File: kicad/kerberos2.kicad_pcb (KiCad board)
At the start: 2 copper layers, 62.5 x 83.8 mm, 15 parts, among them J1 USB4125-GF-A_REVA2, J2 MIDI-in, J3 MIDI-thru, J4 MIDI-out, SW1 TL1105JAF160Q, U1 RP2040, U2 W9812G6KH-6, U3 T8Q144, U4 MX25L25645G

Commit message: first complete test version for Kerberos 2
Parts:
- removed @HOLE0: , 
- removed U$1: , midi:CE-4MM
- removed U$2: , midi:MUELLTONNE_10.00
- removed the U1 at (100.4, 92.0)
- added C1: 100n, Capacitor_SMD:C_0805_2012Metric, F.Cu at (63.7, 79.7)
- added C10: 100n, Capacitor_SMD:C_0805_2012Metric, F.Cu at (63.1, 29.4)
- added C11: 100n, Capacitor_SMD:C_0805_2012Metric, F.Cu at (63.1, 26.4)
- added C12: 100n, Capacitor_SMD:C_0805_2012Metric, F.Cu at (67.6, 23.4)
- added C13: 100n, Capacitor_SMD:C_0805_2012Metric, F.Cu at (138.6, 26.5)
- added C14: 1u, Capacitor_SMD:C_0805_2012Metric, F.Cu at (63.1, 32.5)
- added C15: 4.7u, Capacitor_SMD:C_0805_2012Metric, F.Cu at (27.6, 52.9)
- added C16: 100n, Capacitor_SMD:C_0402_1005Metric, F.Cu at (36.0, 105.9)
- added C17: 100n, Capacitor_SMD:C_0402_1005Metric, F.Cu at (27.6, 58.9)
- added C18: 100n, Capacitor_SMD:C_0402_1005Metric, F.Cu at (33.0, 107.9)
- added C19: 100n, Capacitor_SMD:C_0402_1005Metric, F.Cu at (32.0, 58.9)
- added C2: 10u, Capacitor_SMD:C_0805_2012Metric, F.Cu at (63.1, 23.4)
- added C20: 100n, Capacitor_SMD:C_0402_1005Metric, F.Cu at (27.6, 55.9)
- added C21: 100n, Capacitor_SMD:C_0402_1005Metric, F.Cu at (18.6, 55.6)
- added C22: 100n, Capacitor_SMD:C_0402_1005Metric, F.Cu at (30.1, 107.9)
- added C23: 100n, Capacitor_SMD:C_0402_1005Metric, F.Cu at (23.1, 58.9)
- added C24: 100n, Capacitor_SMD:C_0402_1005Metric, F.Cu at (10.9, 86.4)
- added C25: 100n, Capacitor_SMD:C_0402_1005Metric, F.Cu at (18.6, 61.7)
- added C26: 100n, Capacitor_SMD:C_0402_1005Metric, F.Cu at (23.2, 52.9)
- added C27: 100n, Capacitor_SMD:C_0402_1005Metric, F.Cu at (18.6, 58.6)
- added C28: 100n, Capacitor_SMD:C_0402_1005Metric, F.Cu at (23.1, 55.9)
- added C29: 100n, Capacitor_SMD:C_0402_1005Metric, F.Cu at (32.0, 55.9)
- added C3: 100n, Capacitor_SMD:C_0805_2012Metric, F.Cu at (125.1, 33.9)
- added C30: 100n, Capacitor_SMD:C_0402_1005Metric, F.Cu at (32.1, 52.9)
- added C31: 100n, Capacitor_SMD:C_0402_1005Metric, F.Cu at (132.3, 93.4)
- added C32: 100n, Capacitor_SMD:C_0402_1005Metric, F.Cu at (128.1, 81.4)
- added C33: 100n, Capacitor_SMD:C_0402_1005Metric, F.Cu at (136.8, 90.4)
- added C34: 4.7u, Capacitor_SMD:C_0805_2012Metric, F.Cu at (50.4, 75.3)
- added C35: 10u, Capacitor_SMD:C_0805_2012Metric, F.Cu at (59.1, 81.2)
- added C36: 4.7u, Capacitor_SMD:C_0805_2012Metric, F.Cu at (59.6, 93.0)
- added C37: 10u, Capacitor_SMD:C_0805_2012Metric, F.Cu at (51.4, 87.2)
- added C38: 1n, Capacitor_SMD:C_0805_2012Metric, F.Cu at (148.0, 44.0)
- added C39: 1n, Capacitor_SMD:C_0805_2012Metric, F.Cu at (135.0, 58.7)
- added C4: 100n, Capacitor_SMD:C_0805_2012Metric, F.Cu at (67.6, 26.4)
- added C40: 100n, Capacitor_SMD:C_0805_2012Metric, F.Cu at (153.6, 40.7)
- added C41: 100n, Capacitor_SMD:C_0805_2012Metric, F.Cu at (147.2, 47.3)
- added C5: 100n, Capacitor_SMD:C_0805_2012Metric, F.Cu at (125.1, 30.8)
- added C6: 100n, Capacitor_SMD:C_0805_2012Metric, F.Cu at (129.6, 33.7)
- added C7: 100n, Capacitor_SMD:C_0805_2012Metric, F.Cu at (72.0, 23.4)
- added C8: 100n, Capacitor_SMD:C_0805_2012Metric, F.Cu at (134.0, 33.7)
- added C9: 1u, Capacitor_SMD:C_0805_2012Metric, F.Cu at (138.6, 29.6)
- added D3: ~, LED_THT:LED_D3.0mm, F.Cu at (69.2, 57.8)
- added D4: ~, LED_THT:LED_D3.0mm, F.Cu at (87.5, 57.8)
- added D5: BAV99, Package_TO_SOT_SMD:SOT-23, F.Cu at (130.3, 59.4)
- added D6: BAV99, Package_TO_SOT_SMD:SOT-23, F.Cu at (142.6, 48.0)
- added D7: BAV99, Package_TO_SOT_SMD:SOT-23, F.Cu at (139.7, 52.9)
- added FB1: FerriteBead, Inductor_SMD:L_0805_2012Metric, F.Cu at (77.8, 77.2)
- added FB2: FerriteBead, Inductor_SMD:L_0805_2012Metric, F.Cu at (18.7, 52.8)
- added JP2: host-mode-supply, Connector_PinHeader_2.54mm:PinHeader_1x02_P2.54mm_Vertical, F.Cu at (86.5, 22.6)
- added JP3: 3.3V+, Connector_PinHeader_2.54mm:PinHeader_1x02_P2.54mm_Vertical, F.Cu at (22.2, 90.5)
- added JP4: 3.3V, Connector_PinHeader_2.54mm:PinHeader_1x02_P2.54mm_Vertical, F.Cu at (26.8, 90.5)
- added JP5: 3.3V-, Connector_PinHeader_2.54mm:PinHeader_1x02_P2.54mm_Vertical, F.Cu at (26.8, 83.3)
- added JP6: 1.2V+, Connector_PinHeader_2.54mm:PinHeader_1x02_P2.54mm_Vertical, F.Cu at (31.5, 83.3)
- added JP7: 1.2V, Connector_PinHeader_2.54mm:PinHeader_1x02_P2.54mm_Vertical, F.Cu at (36.1, 83.3)
- added JP8: 1.2V-, Connector_PinHeader_2.54mm:PinHeader_1x02_P2.54mm_Vertical, F.Cu at (22.2, 83.3)
- added JP9: ~{USB_BOOT}, Connector_PinHeader_2.54mm:PinHeader_1x02_P2.54mm_Vertical, F.Cu at (134.0, 27.4)
- added L1: 4.7u, coil:coil, F.Cu at (59.5, 76.1)
- added L2: 4.7u, coil:coil, F.Cu at (51.2, 92.0)
- added Q1: Q_NMOS_GSD, Package_TO_SOT_SMD:SOT-23, F.Cu at (150.7, 108.0)
- added Q10: Q_NMOS_GSD, Package_TO_SOT_SMD:SOT-23, F.Cu at (147.7, 93.0)
- added Q2: Q_NMOS_GSD, Package_TO_SOT_SMD:SOT-23, F.Cu at (144.1, 73.2)
- added Q3: Q_NMOS_GSD, Package_TO_SOT_SMD:SOT-23, F.Cu at (132.7, 69.6)
- added Q4: Q_NMOS_GSD, Package_TO_SOT_SMD:SOT-23, F.Cu at (118.2, 111.1)
- added Q5: Q_NMOS_GSD, Package_TO_SOT_SMD:SOT-23, F.Cu at (38.9, 32.0)
- added Q6: Q_NMOS_GSD, Package_TO_SOT_SMD:SOT-23, F.Cu at (25.3, 31.4)
- added Q7: Q_NMOS_GSD, Package_TO_SOT_SMD:SOT-23, F.Cu at (135.3, 111.1)
- added Q8: Q_NMOS_GSD, Package_TO_SOT_SMD:SOT-23, F.Cu at (154.6, 78.4)
- added Q9: Q_NMOS_GSD, Package_TO_SOT_SMD:SOT-23, F.Cu at (156.3, 66.3)
- added R1: 5.1, Resistor_SMD:R_0805_2012Metric, F.Cu at (91.1, 21.8)
- added R10: 22, Resistor_SMD:R_0805_2012Metric, F.Cu at (95.5, 21.8)
- added R11: 22, Resistor_SMD:R_0805_2012Metric, F.Cu at (99.6, 27.6)
- added R12: 22, Resistor_SMD:R_0805_2012Metric, F.Cu at (104.3, 24.7)
- added R13: 22, Resistor_SMD:R_0805_2012Metric, F.Cu at (95.2, 33.5)
- added R14: 22, Resistor_SMD:R_0805_2012Metric, F.Cu at (99.9, 21.8)
- added R15: 22, Resistor_SMD:R_0805_2012Metric, F.Cu at (104.0, 27.6)
- added R16: 22, Resistor_SMD:R_0805_2012Metric, F.Cu at (108.7, 24.7)
- added R17: 22, Resistor_SMD:R_0805_2012Metric, F.Cu at (99.6, 30.6)
- added R18: 22, Resistor_SMD:R_0805_2012Metric, F.Cu at (95.2, 27.6)
- added R19: 22, Resistor_SMD:R_0805_2012Metric, F.Cu at (108.7, 21.8)
- added R2: 5.1, Resistor_SMD:R_0805_2012Metric, F.Cu at (91.1, 24.7)
- added R20: 1k, Resistor_SMD:R_0805_2012Metric, F.Cu at (104.3, 21.8)
- added R21: 1k, Resistor_SMD:R_0805_2012Metric, F.Cu at (90.8, 31.9)
- added R22: 10k, Resistor_SMD:R_0805_2012Metric, F.Cu at (143.0, 26.6)
- added R23: 10k, Resistor_SMD:R_0805_2012Metric, F.Cu at (138.4, 33.7)
- added R24: 1k, Resistor_SMD:R_0805_2012Metric, F.Cu at (67.5, 29.4)
- added R25: 10k, Resistor_SMD:R_0805_2012Metric, F.Cu at (72.0, 26.4)
- added R26: 10k, Resistor_SMD:R_0402_1005Metric, F.Cu at (30.1, 105.9)
- added R27: 10k, Resistor_SMD:R_0402_1005Metric, F.Cu at (118.1, 66.1)
- added R28: 10k, Resistor_SMD:R_0402_1005Metric, F.Cu at (33.1, 105.9)
- added R29: 10k, Resistor_SMD:R_0402_1005Metric, F.Cu at (118.1, 70.1)
- added R3: 27, Resistor_SMD:R_0805_2012Metric, F.Cu at (81.6, 81.9)
- added R30: 10k, Resistor_SMD:R_0402_1005Metric, F.Cu at (118.1, 68.1)
- added R31: 10k, Resistor_SMD:R_0402_1005Metric, F.Cu at (121.0, 68.1)
- added R32: 10k, Resistor_SMD:R_0402_1005Metric, F.Cu at (121.0, 66.1)
- added R33: 10k, Resistor_SMD:R_0402_1005Metric, F.Cu at (132.3, 102.3)
- added R34: 10k, Resistor_SMD:R_0402_1005Metric, F.Cu at (136.8, 93.4)
- added R35: 1k, Resistor_SMD:R_0402_1005Metric, F.Cu at (132.3, 99.3)
- added R36: 1k, Resistor_SMD:R_0402_1005Metric, F.Cu at (132.3, 96.4)
- added R37: 10k, Resistor_SMD:R_0402_1005Metric, F.Cu at (136.7, 99.3)
- added R38: 10k, Resistor_SMD:R_0402_1005Metric, F.Cu at (136.8, 96.3)
- added R39: 10k, Resistor_SMD:R_0402_1005Metric, F.Cu at (149.7, 111.2)
- added R4: 27, Resistor_SMD:R_0805_2012Metric, F.Cu at (95.2, 30.6)
- added R40: R, Resistor_SMD:R_0402_1005Metric, F.Cu at (55.0, 79.0)
- added R41: R, Resistor_SMD:R_0402_1005Metric, F.Cu at (51.0, 79.0)
- added R42: R, Resistor_SMD:R_0402_1005Metric, F.Cu at (55.5, 89.6)
- added R43: R, Resistor_SMD:R_0402_1005Metric, F.Cu at (59.9, 89.6)
- added R44: 220, Resistor_SMD:R_1206_3216Metric, F.Cu at (134.5, 52.3)
- added R45: 220, Resistor_SMD:R_1206_3216Metric, F.Cu at (134.5, 55.6)
- added R46: 220, Resistor_SMD:R_1206_3216Metric, F.Cu at (125.0, 58.6)
- added R47: 220, Resistor_SMD:R_1206_3216Metric, F.Cu at (148.5, 40.8)
- added R48: 220, Resistor_SMD:R_1206_3216Metric, F.Cu at (142.9, 44.1)
- added R49: 10k, Resistor_SMD:R_0805_2012Metric, F.Cu at (139.5, 56.5)
- added R5: 27, Resistor_SMD:R_0805_2012Metric, F.Cu at (99.9, 24.7)
- added R50: 220, Resistor_SMD:R_1206_3216Metric, F.Cu at (119.4, 58.6)
- added R51: 220, Resistor_SMD:R_1206_3216Metric, F.Cu at (142.9, 40.8)
- added R52: 1k8, Resistor_SMD:R_0805_2012Metric, F.Cu at (152.4, 43.9)
- added R53: 3k3, Resistor_SMD:R_0805_2012Metric, F.Cu at (144.4, 51.7)
- added R54: 10k, Resistor_SMD:R_0402_1005Metric, F.Cu at (143.1, 76.5)
- added R55: 10k, Resistor_SMD:R_0402_1005Metric, F.Cu at (131.7, 72.8)
- added R56: 10k, Resistor_SMD:R_0402_1005Metric, F.Cu at (117.2, 114.3)
- added R57: 10k, Resistor_SMD:R_0402_1005Metric, F.Cu at (37.9, 35.2)
- added R58: 10k, Resistor_SMD:R_0402_1005Metric, F.Cu at (24.3, 34.6)
- added R59: 10k, Resistor_SMD:R_0402_1005Metric, F.Cu at (134.3, 114.3)
- added R6: 27, Resistor_SMD:R_0805_2012Metric, F.Cu at (86.4, 28.9)
- added R60: 10k, Resistor_SMD:R_0402_1005Metric, F.Cu at (153.6, 81.6)
- added R61: 10k, Resistor_SMD:R_0402_1005Metric, F.Cu at (155.4, 69.5)
- added R62: 10k, Resistor_SMD:R_0402_1005Metric, F.Cu at (146.7, 96.2)
- added R7: 22, Resistor_SMD:R_0805_2012Metric, F.Cu at (86.4, 31.9)
- added R8: 22, Resistor_SMD:R_0805_2012Metric, F.Cu at (90.8, 28.9)
- added R9: 22, Resistor_SMD:R_0805_2012Metric, F.Cu at (95.5, 24.7)
- added RN1: 33, resistor-network:16P8, F.Cu at (63.0, 108.3)
- added RN2: 33, resistor-network:16P8, F.Cu at (68.9, 108.3)
- added RN3: 33, resistor-network:16P8, F.Cu at (84.5, 108.8)
- added RN4: 33, resistor-network:16P8, F.Cu at (75.3, 108.3)
- added RN5: 33, resistor-network:16P8, F.Cu at (91.8, 109.0)
- added SW2: SKRPADE010, button:KEY-SMD_4P-L4.2-W3.2-P2.20-LS4.6, F.Cu at (119.8, 31.5)
- added U10: 6N138, 6N138S:6N138S, F.Cu at (60.0, 65.9)
- added U11: 74LS14, Package_SO:SOIC-14_3.9x8.7mm_P1.27mm, F.Cu at (70.4, 76.4)
- added U4: 74ALVC164245DGG,51, Package_SO:TSSOP-48_8x12.5mm_P0.5mm, F.Cu at (88.9, 96.2)
- added U5: GW1NR-4&4B_QN881, qn88:QFN-88_EP_10x10_Pitch0.4mm, F.Cu at (71.5, 86.9)
- added U6: AD8694ARZ, Package_SO:SOIC-14_3.9x8.7mm_P1.27mm, F.Cu at (99.2, 64.2)
- added U7: TMCS1108A3UQDR, Package_SO:SOIC-8_3.9x4.9mm_P1.27mm, F.Cu at (88.9, 68.4)
- added U8: M3406, Package_TO_SOT_SMD:TSOT-23-5, F.Cu at (54.3, 75.3)
- added U9: M3406, Package_TO_SOT_SMD:TSOT-23-5, F.Cu at (55.8, 93.0)
- added USB1: TYPEC-304J-BCP16, usb-c:USB-C-SMD_TYPEC-304J-BCP16, F.Cu at (102.6, 89.1)
- added X1: SX3M12.000M20F30TNN, oscillator:SX3M12.000M20F30TNN, F.Cu at (81.3, 78.0)
- D1, D2: value LED -> D_Schottky; footprint LED_THT:LED_D3.0mm -> Diode_SMD:D_SMA
- J1: value USB4125-GF-A_REVA2 -> 503398-1892; footprint usb-c:GCT_USB4125-GF-A_REVA2 -> sd-card:MOLEX_503398-1892
- SW1: value TL1105JAF160Q -> side-button
- U2: value W9812G6KH-6 -> RP2040; footprint Package_SO:TSOP-II-54_22.2x10.16mm_P0.8mm -> rp2040:QFN40P700X700X90-57N
- U3: value T8Q144 -> 74ALVC164245DGG,51; footprint Package_QFP:LQFP-144_20x20mm_P0.5mm -> Package_SO:TSSOP-48_8x12.5mm_P0.5mm
- moved D2 56.9 mm to (54.3, 104.0), turned to -90 degrees
- moved D1 52.9 mm to (100.3, 100.6), turned to 90 degrees
- moved U2 32.3 mm to (88.9, 81.2)
- moved U1 12.5 mm to (78.6, 68.7)
- moved U3 10.9 mm to (70.7, 99.9), turned to 90 degrees
- moved J1 5.22 mm to (100.6, 76.0)
- moved J4 0.05 mm to (95.3, 50.2)
- renumbered U4 to U1
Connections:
- D1 pad 1: unconnected-(D1-Pad1) -> +5V
- D1 pad 2: unconnected-(D1-Pad2) -> Net-(D1-Pad2)
- D2 pad 1: unconnected-(D2-Pad1) -> +5V
- D2 pad 2: unconnected-(D2-Pad2) -> Net-(D2-Pad2)
- J2 pad 4: unconnected-(J2-Pad4) -> Net-(J2-Pad4)
- J2 pad 5: unconnected-(J2-Pad5) -> Net-(D5-Pad1)
- J3 pad 2: unconnected-(J3-Pad2) -> GND
- J3 pad 4: unconnected-(J3-Pad4) -> Net-(J3-Pad4)
- J3 pad 5: unconnected-(J3-Pad5) -> Net-(C38-Pad1)
- J3 pad S: unconnected-(J3-PadS) -> GND
- J4 pad 2: unconnected-(J4-Pad2) -> GND
- J4 pad 4: unconnected-(J4-Pad4) -> Net-(J4-Pad4)
- J4 pad 5: unconnected-(J4-Pad5) -> Net-(C39-Pad1)
- J4 pad S: unconnected-(J4-PadS) -> GND
- JP1 pad 1: unconnected-(JP1-Pad1) -> GND
- JP1 pad 10: unconnected-(JP1-Pad10) -> Net-(JP1-Pad10)
- JP1 pad 11: unconnected-(JP1-Pad11) -> Net-(JP1-Pad11)
- JP1 pad 12: unconnected-(JP1-Pad12) -> Net-(JP1-Pad12)
- JP1 pad 13: unconnected-(JP1-Pad13) -> Net-(JP1-Pad13)
- JP1 pad 14: unconnected-(JP1-Pad14) -> Net-(JP1-Pad14)
- JP1 pad 15: unconnected-(JP1-Pad15) -> Net-(JP1-Pad15)
- JP1 pad 16: unconnected-(JP1-Pad16) -> Net-(JP1-Pad16)
- JP1 pad 17: unconnected-(JP1-Pad17) -> Net-(JP1-Pad17)
- JP1 pad 18: unconnected-(JP1-Pad18) -> Net-(JP1-Pad18)
- JP1 pad 19: unconnected-(JP1-Pad19) -> Net-(JP1-Pad19)
- JP1 pad 2: unconnected-(JP1-Pad2) -> Net-(D2-Pad2)
- JP1 pad 20: unconnected-(JP1-Pad20) -> Net-(JP1-Pad20)
- JP1 pad 21: unconnected-(JP1-Pad21) -> Net-(JP1-Pad21)
- JP1 pad 22: unconnected-(JP1-Pad22) -> GND
- JP1 pad 3: unconnected-(JP1-Pad3) -> Net-(D2-Pad2)
- JP1 pad 4: unconnected-(JP1-Pad4) -> Net-(JP1-Pad4)
- JP1 pad 5: unconnected-(JP1-Pad5) -> Net-(JP1-Pad5)
- JP1 pad 6: unconnected-(JP1-Pad6) -> Net-(JP1-Pad6)
- JP1 pad 7: unconnected-(JP1-Pad7) -> Net-(JP1-Pad7)
- JP1 pad 8: unconnected-(JP1-Pad8) -> Net-(JP1-Pad8)
- JP1 pad 9: unconnected-(JP1-Pad9) -> Net-(JP1-Pad9)
- JP1 pad A: unconnected-(JP1-PadA) -> GND
- JP1 pad B: unconnected-(JP1-PadB) -> Net-(JP1-PadB)
- JP1 pad C: unconnected-(JP1-PadC) -> Net-(JP1-PadC)
- JP1 pad D: unconnected-(JP1-PadD) -> Net-(JP1-PadD)
- JP1 pad E: unconnected-(JP1-PadE) -> Net-(JP1-PadE)
- JP1 pad F: unconnected-(JP1-PadF) -> Net-(JP1-PadF)
- JP1 pad H: unconnected-(JP1-PadH) -> Net-(JP1-PadH)
- JP1 pad J: unconnected-(JP1-PadJ) -> Net-(JP1-PadJ)
- JP1 pad K: unconnected-(JP1-PadK) -> Net-(JP1-PadK)
- JP1 pad L: unconnected-(JP1-PadL) -> Net-(JP1-PadL)
- JP1 pad M: unconnected-(JP1-PadM) -> Net-(JP1-PadM)
- JP1 pad N: unconnected-(JP1-PadN) -> Net-(JP1-PadN)
- JP1 pad P: unconnected-(JP1-PadP) -> Net-(JP1-PadP)
- JP1 pad R: unconnected-(JP1-PadR) -> Net-(JP1-PadR)
- JP1 pad S: unconnected-(JP1-PadS) -> Net-(JP1-PadS)
- JP1 pad T: unconnected-(JP1-PadT) -> Net-(JP1-PadT)
- JP1 pad U: unconnected-(JP1-PadU) -> Net-(JP1-PadU)
- JP1 pad V: unconnected-(JP1-PadV) -> Net-(JP1-PadV)
- JP1 pad W: unconnected-(JP1-PadW) -> Net-(JP1-PadW)
- JP1 pad X: unconnected-(JP1-PadX) -> Net-(JP1-PadX)
- JP1 pad Y: unconnected-(JP1-PadY) -> Net-(JP1-PadY)
- JP1 pad Z: unconnected-(JP1-PadZ) -> GND
- SW1 pad 1: unconnected-(SW1-Pad1) -> GND
- SW1 pad 2: unconnected-(SW1-Pad2) -> Net-(R22-Pad2)
- U1 pad 1: unconnected-(U4-Pad1) -> /GW1NR FPGA/FLASH_CS
- U1 pad 2: unconnected-(U4-Pad2) -> /GW1NR FPGA/FLASH-SIO1
- U1 pad 3: unconnected-(U4-Pad3) -> /GW1NR FPGA/FLASH-SIO2
- U1 pad 4: unconnected-(U4-Pad4) -> GND
- U1 pad 5: unconnected-(U4-Pad5) -> /GW1NR FPGA/FLASH-SIO0
- U1 pad 6: unconnected-(U4-Pad6) -> /GW1NR FPGA/FLASH-SCLK
- U1 pad 7: unconnected-(U4-Pad7) -> /GW1NR FPGA/FLASH-SIO3
- U1 pad 8: unconnected-(U4-Pad8) -> +3.3V
- U2 pad 1: Net-(U2-Pad1) -> +3.3V
- U2 pad 10: unconnected-(U2-Pad10) -> +3.3V
- U2 pad 11: unconnected-(U2-Pad11) -> /RP2040 microcontroller/spare2
- U2 pad 12: Net-(U2-Pad12) -> /RP2040 microcontroller/spare3
- U2 pad 13: unconnected-(U2-Pad13) -> /RP2040 microcontroller/spare4
- U2 pad 14: Net-(U2-Pad1) -> /RP2040 microcontroller/spare5
- U2 pad 15: unconnected-(U2-Pad15) -> /RP2040 microcontroller/spare6
- U2 pad 16: unconnected-(U2-Pad16) -> Net-(R22-Pad2)
- U2 pad 19: unconnected-(U2-Pad19) -> GND
- U2 pad 2: unconnected-(U2-Pad2) -> /RP2040 microcontroller/JTAGSEL_N
- U2 pad 20: unconnected-(U2-Pad20) -> /RP2040 microcontroller/XIN
- U2 pad 22: unconnected-(U2-Pad22) -> +3.3V
- U2 pad 23: unconnected-(U2-Pad23) -> /RP2040 microcontroller/1.1V
- U2 pad 26: unconnected-(U2-Pad26) -> Net-(R23-Pad1)
- U2 pad 27: Net-(U2-Pad1) -> unconnected-(U2-Pad27)
- U2 pad 28: Net-(U2-Pad28) -> unconnected-(U2-Pad28)
- U2 pad 3: Net-(U2-Pad3) -> /RP2040 microcontroller/TCK
- U2 pad 30: unconnected-(U2-Pad30) -> Net-(J1-Pad3)
- U2 pad 31: unconnected-(U2-Pad31) -> Net-(J1-Pad5)
- U2 pad 32: unconnected-(U2-Pad32) -> Net-(J1-Pad7)
- U2 pad 33: unconnected-(U2-Pad33) -> +3.3V
- U2 pad 34: unconnected-(U2-Pad34) -> Net-(J1-Pad8)
- U2 pad 35: unconnected-(U2-Pad35) -> Net-(J1-Pad1)
- U2 pad 36: unconnected-(U2-Pad36) -> Net-(J1-Pad2)
- U2 pad 37: unconnected-(U2-Pad37) -> Net-(J1-Pad10)
- U2 pad 4: unconnected-(U2-Pad4) -> /RP2040 microcontroller/TMS
- U2 pad 41: Net-(U2-Pad28) -> unconnected-(U2-Pad41)
- U2 pad 42: unconnected-(U2-Pad42) -> +3.3V
- U2 pad 43: Net-(U2-Pad3) -> +3.3V
- U2 pad 44: unconnected-(U2-Pad44) -> +3.3V
- U2 pad 45: unconnected-(U2-Pad45) -> /RP2040 microcontroller/1.1V
- U2 pad 46: Net-(U2-Pad12) -> /RP2040 microcontroller/USB_D-
- U2 pad 47: unconnected-(U2-Pad47) -> /RP2040 microcontroller/USB_D+
- U2 pad 48: unconnected-(U2-Pad48) -> +3.3V
- U2 pad 49: Net-(U2-Pad3) -> +3.3V
- U2 pad 5: unconnected-(U2-Pad5) -> /RP2040 microcontroller/TDO
- U2 pad 50: unconnected-(U2-Pad50) -> /RP2040 microcontroller/1.1V
- U2 pad 51: unconnected-(U2-Pad51) -> /GW1NR FPGA/FLASH-SIO3
- U2 pad 52: Net-(U2-Pad12) -> /GW1NR FPGA/FLASH-SCLK
- U2 pad 53: unconnected-(U2-Pad53) -> /GW1NR FPGA/FLASH-SIO0
- U2 pad 54: Net-(U2-Pad28) -> /GW1NR FPGA/FLASH-SIO2
- U2 pad 6: Net-(U2-Pad12) -> /RP2040 microcontroller/TDI
- U2 pad 7: unconnected-(U2-Pad7) -> /RP2040 microcontroller/DONE
- U2 pad 8: unconnected-(U2-Pad8) -> /RP2040 microcontroller/RECONFIG_N
- U2 pad 9: Net-(U2-Pad3) -> /RP2040 microcontroller/spare1
- U3 pad 1: unconnected-(U3-Pad1) -> /GW1NR FPGA/DIR_A
- U3 pad 10: unconnected-(U3-Pad10) -> GND
- U3 pad 11: unconnected-(U3-Pad11) -> /GW1NR FPGA/A6
- U3 pad 12: unconnected-(U3-Pad12) -> /GW1NR FPGA/A7
- U3 pad 13: unconnected-(U3-Pad13) -> /GW1NR FPGA/A8
- U3 pad 14: unconnected-(U3-Pad14) -> /GW1NR FPGA/A9
- U3 pad 15: unconnected-(U3-Pad15) -> GND
- U3 pad 16: unconnected-(U3-Pad16) -> /GW1NR FPGA/A10
- U3 pad 17: unconnected-(U3-Pad17) -> /GW1NR FPGA/A11
- U3 pad 18: unconnected-(U3-Pad18) -> +5V
- U3 pad 19: unconnected-(U3-Pad19) -> /GW1NR FPGA/A12
- U3 pad 2: unconnected-(U3-Pad2) -> /GW1NR FPGA/A0
- U3 pad 20: unconnected-(U3-Pad20) -> /GW1NR FPGA/A13
- U3 pad 21: unconnected-(U3-Pad21) -> GND
- U3 pad 22: unconnected-(U3-Pad22) -> /GW1NR FPGA/A14
- U3 pad 23: unconnected-(U3-Pad23) -> /GW1NR FPGA/A15
- U3 pad 24: unconnected-(U3-Pad24) -> /GW1NR FPGA/DIR_A
- U3 pad 25: unconnected-(U3-Pad25) -> GND
- U3 pad 26: unconnected-(U3-Pad26) -> /GW1NR FPGA/A15_t
- U3 pad 27: unconnected-(U3-Pad27) -> /GW1NR FPGA/A14_t
- U3 pad 28: unconnected-(U3-Pad28) -> GND
- U3 pad 29: unconnected-(U3-Pad29) -> /GW1NR FPGA/A13_t
- U3 pad 3: unconnected-(U3-Pad3) -> /GW1NR FPGA/A1
- U3 pad 30: unconnected-(U3-Pad30) -> /GW1NR FPGA/A12_t
- U3 pad 31: unconnected-(U3-Pad31) -> +3.3V
- U3 pad 32: unconnected-(U3-Pad32) -> /GW1NR FPGA/A11_t
- U3 pad 33: unconnected-(U3-Pad33) -> /GW1NR FPGA/A10_t
- U3 pad 34: unconnected-(U3-Pad34) -> GND
- U3 pad 35: unconnected-(U3-Pad35) -> /GW1NR FPGA/A9_t
- U3 pad 36: unconnected-(U3-Pad36) -> /GW1NR FPGA/A8_t
- U3 pad 37: unconnected-(U3-Pad37) -> /GW1NR FPGA/A7_t
- U3 pad 38: unconnected-(U3-Pad38) -> /GW1NR FPGA/A6_t
- U3 pad 39: unconnected-(U3-Pad39) -> GND
- U3 pad 4: unconnected-(U3-Pad4) -> GND
- U3 pad 40: unconnected-(U3-Pad40) -> /GW1NR FPGA/A5_t
- U3 pad 41: unconnected-(U3-Pad41) -> /GW1NR FPGA/A4_t
- U3 pad 42: unconnected-(U3-Pad42) -> +3.3V
- U3 pad 43: unconnected-(U3-Pad43) -> /GW1NR FPGA/A3_t
- U3 pad 44: unconnected-(U3-Pad44) -> /GW1NR FPGA/A2_t
- U3 pad 45: unconnected-(U3-Pad45) -> GND
- U3 pad 46: unconnected-(U3-Pad46) -> /GW1NR FPGA/A1_t
- U3 pad 47: unconnected-(U3-Pad47) -> /GW1NR FPGA/A0_t
- U3 pad 48: unconnected-(U3-Pad48) -> GND
- U3 pad 5: unconnected-(U3-Pad5) -> /GW1NR FPGA/A2
- U3 pad 6: unconnected-(U3-Pad6) -> /GW1NR FPGA/A3
- U3 pad 7: unconnected-(U3-Pad7) -> +5V
- U3 pad 8: unconnected-(U3-Pad8) -> /GW1NR FPGA/A4
- U3 pad 9: unconnected-(U3-Pad9) -> /GW1NR FPGA/A5

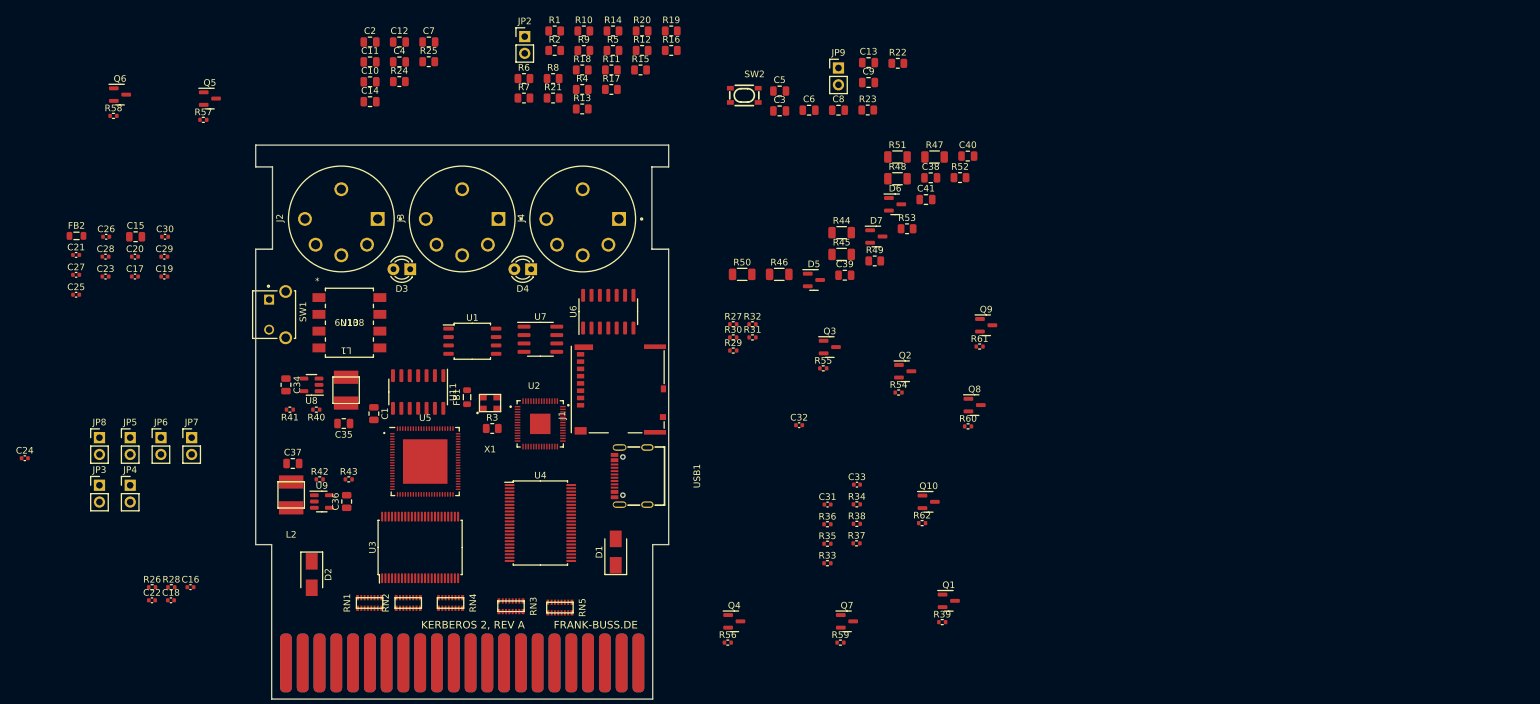
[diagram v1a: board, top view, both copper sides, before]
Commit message: new flash, and IEC interface added
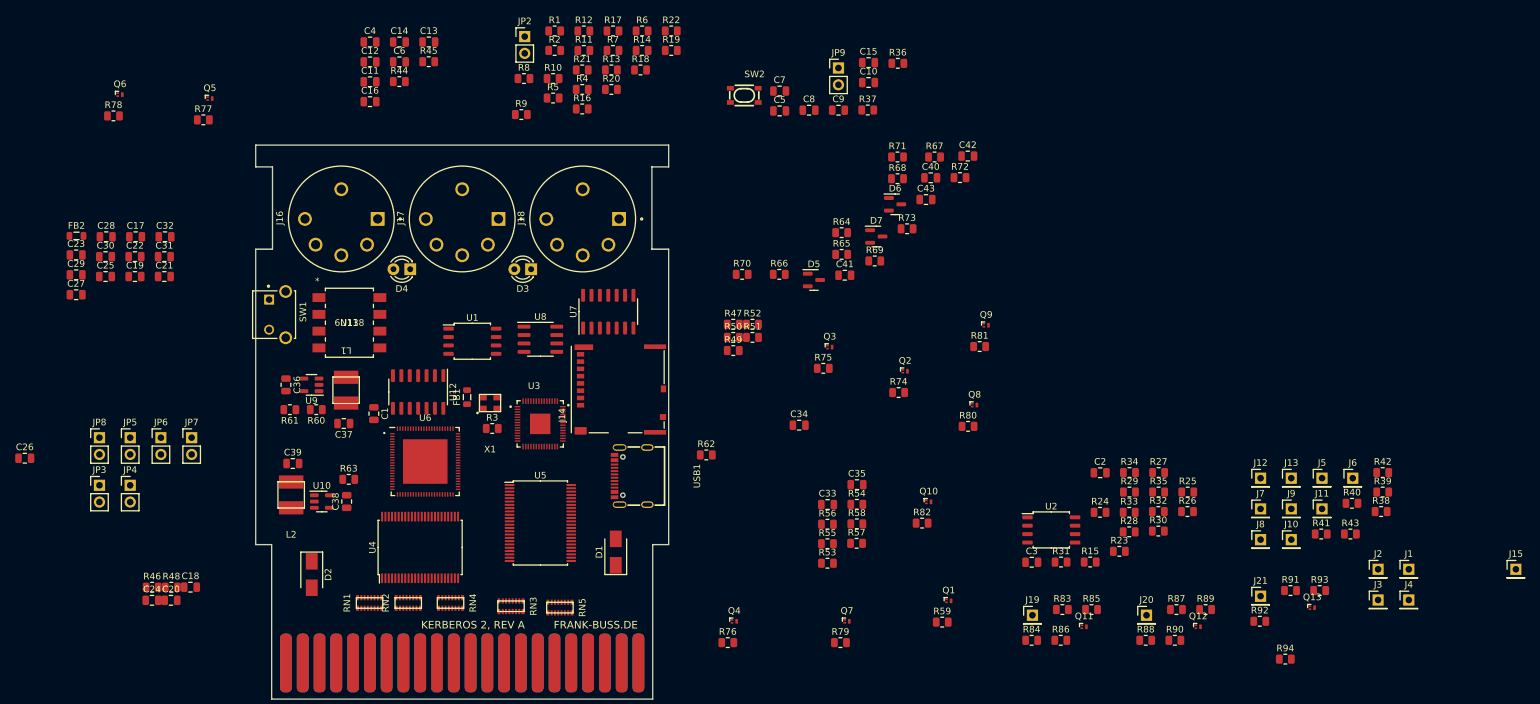
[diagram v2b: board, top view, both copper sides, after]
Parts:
- added C2: 100n, Capacitor_SMD:C_0805_2012Metric, F.Cu at (173.6, 88.6)
- added C3: 100n, Capacitor_SMD:C_0805_2012Metric, F.Cu at (163.2, 102.1)
- added J1: 5V, Connector_PinHeader_2.54mm:PinHeader_1x01_P2.54mm_Vertical, F.Cu at (220.3, 103.2)
- added J10: rp_spare3, Connector_PinHeader_2.54mm:PinHeader_1x01_P2.54mm_Vertical, F.Cu at (202.5, 98.7)
- added J11: rp_spare4, Connector_PinHeader_2.54mm:PinHeader_1x01_P2.54mm_Vertical, F.Cu at (207.2, 94.1)
- added J12: rp_spare5, Connector_PinHeader_2.54mm:PinHeader_1x01_P2.54mm_Vertical, F.Cu at (197.9, 89.4)
- added J13: rp_spare6, Connector_PinHeader_2.54mm:PinHeader_1x01_P2.54mm_Vertical, F.Cu at (202.5, 89.4)
- added J15: fpga_spare, Connector_PinHeader_2.54mm:PinHeader_1x01_P2.54mm_Vertical, F.Cu at (236.5, 103.2)
- added J19: IEC, Connector_PinHeader_2.54mm:PinHeader_1x01_P2.54mm_Vertical, F.Cu at (163.3, 110.2)
- added J2: 3.3V, Connector_PinHeader_2.54mm:PinHeader_1x01_P2.54mm_Vertical, F.Cu at (215.7, 103.2)
- added J20: IEC, Connector_PinHeader_2.54mm:PinHeader_1x01_P2.54mm_Vertical, F.Cu at (180.6, 110.2)
- added J21: IEC, Connector_PinHeader_2.54mm:PinHeader_1x01_P2.54mm_Vertical, F.Cu at (197.9, 107.3)
- added J3: 1.2V, Connector_PinHeader_2.54mm:PinHeader_1x01_P2.54mm_Vertical, F.Cu at (215.7, 107.8)
- added J4: GND, Connector_PinHeader_2.54mm:PinHeader_1x01_P2.54mm_Vertical, F.Cu at (220.3, 107.8)
- added J5: SWCLK, Connector_PinHeader_2.54mm:PinHeader_1x01_P2.54mm_Vertical, F.Cu at (207.2, 89.4)
- added J6: SWD, Connector_PinHeader_2.54mm:PinHeader_1x01_P2.54mm_Vertical, F.Cu at (211.8, 89.4)
- added J7: xout, Connector_PinHeader_2.54mm:PinHeader_1x01_P2.54mm_Vertical, F.Cu at (197.9, 94.1)
- added J8: rp_spare1, Connector_PinHeader_2.54mm:PinHeader_1x01_P2.54mm_Vertical, F.Cu at (197.9, 98.7)
- added J9: rp_spare2, Connector_PinHeader_2.54mm:PinHeader_1x01_P2.54mm_Vertical, F.Cu at (202.5, 94.1)
- added Q11: Q_NMOS_GSD, Package_DFN_QFN:Diodes_DFN1006-3, F.Cu at (171.2, 111.9)
- added Q12: Q_NMOS_GSD, Package_DFN_QFN:Diodes_DFN1006-3, F.Cu at (188.4, 111.9)
- added Q13: Q_NMOS_GSD, Package_DFN_QFN:Diodes_DFN1006-3, F.Cu at (205.7, 109.0)
- added R15: 27, Resistor_SMD:R_0805_2012Metric, F.Cu at (172.1, 102.1)
- added R23: 27, Resistor_SMD:R_0805_2012Metric, F.Cu at (176.5, 100.5)
- added R24: 27, Resistor_SMD:R_0805_2012Metric, F.Cu at (173.6, 94.6)
- added R25: 27, Resistor_SMD:R_0805_2012Metric, F.Cu at (186.8, 91.5)
- added R26: 27, Resistor_SMD:R_0805_2012Metric, F.Cu at (186.8, 94.5)
- added R27: 27, Resistor_SMD:R_0805_2012Metric, F.Cu at (182.4, 88.6)
- added R28: 27, Resistor_SMD:R_0805_2012Metric, F.Cu at (178.0, 97.5)
- added R29: 27, Resistor_SMD:R_0805_2012Metric, F.Cu at (178.0, 91.5)
- added R30: 27, Resistor_SMD:R_0805_2012Metric, F.Cu at (182.4, 97.4)
- added R31: 27, Resistor_SMD:R_0805_2012Metric, F.Cu at (167.7, 102.1)
- added R32: 27, Resistor_SMD:R_0805_2012Metric, F.Cu at (182.4, 94.5)
- added R33: 27, Resistor_SMD:R_0805_2012Metric, F.Cu at (178.0, 94.6)
- added R34: 27, Resistor_SMD:R_0805_2012Metric, F.Cu at (178.0, 88.6)
- added R35: 10k, Resistor_SMD:R_0805_2012Metric, F.Cu at (182.4, 91.5)
- added R38: 27, Resistor_SMD:R_0805_2012Metric, F.Cu at (216.1, 94.5)
- added R39: 27, Resistor_SMD:R_0805_2012Metric, F.Cu at (216.3, 91.5)
- added R40: 27, Resistor_SMD:R_0805_2012Metric, F.Cu at (211.7, 93.2)
- added R41: 27, Resistor_SMD:R_0805_2012Metric, F.Cu at (207.1, 97.9)
- added R42: 27, Resistor_SMD:R_0805_2012Metric, F.Cu at (216.3, 88.6)
- added R43: 27, Resistor_SMD:R_0805_2012Metric, F.Cu at (211.5, 97.9)
- added R83: 10k, Resistor_SMD:R_0805_2012Metric, F.Cu at (167.9, 109.3)
- added R84: 27, Resistor_SMD:R_0805_2012Metric, F.Cu at (163.2, 114.0)
- added R85: 10k, Resistor_SMD:R_0805_2012Metric, F.Cu at (172.3, 109.3)
- added R86: 22k, Resistor_SMD:R_0805_2012Metric, F.Cu at (167.6, 114.0)
- added R87: 10k, Resistor_SMD:R_0805_2012Metric, F.Cu at (185.1, 109.3)
- added R88: 27, Resistor_SMD:R_0805_2012Metric, F.Cu at (180.5, 114.0)
- added R89: 10k, Resistor_SMD:R_0805_2012Metric, F.Cu at (189.6, 109.3)
- added R90: 22k, Resistor_SMD:R_0805_2012Metric, F.Cu at (184.9, 114.0)
- added R91: 10k, Resistor_SMD:R_0805_2012Metric, F.Cu at (202.4, 106.4)
- added R92: 27, Resistor_SMD:R_0805_2012Metric, F.Cu at (197.8, 111.1)
- added R93: 10k, Resistor_SMD:R_0805_2012Metric, F.Cu at (206.8, 106.4)
- added R94: 22k, Resistor_SMD:R_0805_2012Metric, F.Cu at (201.6, 116.8)
- added U2: MX25L25645G, Package_SO:SOP-8_5.28x5.23mm_P1.27mm, F.Cu at (166.2, 97.2)
- C18: renamed from C16; footprint Capacitor_SMD:C_0402_1005Metric -> Capacitor_SMD:C_0805_2012Metric
- C19: renamed from C17; footprint Capacitor_SMD:C_0402_1005Metric -> Capacitor_SMD:C_0805_2012Metric
- C20: renamed from C18; footprint Capacitor_SMD:C_0402_1005Metric -> Capacitor_SMD:C_0805_2012Metric
- C21: renamed from C19; footprint Capacitor_SMD:C_0402_1005Metric -> Capacitor_SMD:C_0805_2012Metric
- C22: renamed from C20; footprint Capacitor_SMD:C_0402_1005Metric -> Capacitor_SMD:C_0805_2012Metric
- C23: renamed from C21; footprint Capacitor_SMD:C_0402_1005Metric -> Capacitor_SMD:C_0805_2012Metric
- C24: renamed from C22; footprint Capacitor_SMD:C_0402_1005Metric -> Capacitor_SMD:C_0805_2012Metric
- C25: renamed from C23; footprint Capacitor_SMD:C_0402_1005Metric -> Capacitor_SMD:C_0805_2012Metric
- C26: renamed from C24; footprint Capacitor_SMD:C_0402_1005Metric -> Capacitor_SMD:C_0805_2012Metric
- C27: renamed from C25; footprint Capacitor_SMD:C_0402_1005Metric -> Capacitor_SMD:C_0805_2012Metric
- C28: renamed from C26; footprint Capacitor_SMD:C_0402_1005Metric -> Capacitor_SMD:C_0805_2012Metric
- C29: renamed from C27; footprint Capacitor_SMD:C_0402_1005Metric -> Capacitor_SMD:C_0805_2012Metric
- C30: renamed from C28; footprint Capacitor_SMD:C_0402_1005Metric -> Capacitor_SMD:C_0805_2012Metric
- C31: renamed from C29; footprint Capacitor_SMD:C_0402_1005Metric -> Capacitor_SMD:C_0805_2012Metric
- C32: renamed from C30; footprint Capacitor_SMD:C_0402_1005Metric -> Capacitor_SMD:C_0805_2012Metric
- C33: renamed from C31; footprint Capacitor_SMD:C_0402_1005Metric -> Capacitor_SMD:C_0805_2012Metric
- C34: renamed from C32; footprint Capacitor_SMD:C_0402_1005Metric -> Capacitor_SMD:C_0805_2012Metric
- C35: renamed from C33; footprint Capacitor_SMD:C_0402_1005Metric -> Capacitor_SMD:C_0805_2012Metric
- Q1, Q10, Q2, Q3, Q4, Q5, Q6, Q7, Q8, Q9: footprint Package_TO_SOT_SMD:SOT-23 -> Package_DFN_QFN:Diodes_DFN1006-3
- R10: renamed from R8; value 22 -> 27
- R11: renamed from R9; value 22 -> 27
- R12: renamed from R10; value 22 -> 27
- R13: renamed from R11; value 22 -> 27
- R14: renamed from R12; value 22 -> 27
- R16: renamed from R13; value 22 -> 27
- R17: renamed from R14; value 22 -> 27
- R18: renamed from R15; value 22 -> 27
- R19: renamed from R16; value 22 -> 27
- R20: renamed from R17; value 22 -> 27
- R21: renamed from R18; value 22 -> 27
- R22: renamed from R19; value 22 -> 27
- R46: renamed from R26; footprint Resistor_SMD:R_0402_1005Metric -> Resistor_SMD:R_0805_2012Metric
- R47: renamed from R27; footprint Resistor_SMD:R_0402_1005Metric -> Resistor_SMD:R_0805_2012Metric
- R48: renamed from R28; footprint Resistor_SMD:R_0402_1005Metric -> Resistor_SMD:R_0805_2012Metric
- R49: renamed from R29; footprint Resistor_SMD:R_0402_1005Metric -> Resistor_SMD:R_0805_2012Metric
- R50: renamed from R30; footprint Resistor_SMD:R_0402_1005Metric -> Resistor_SMD:R_0805_2012Metric
- R51: renamed from R31; footprint Resistor_SMD:R_0402_1005Metric -> Resistor_SMD:R_0805_2012Metric
- R52: renamed from R32; footprint Resistor_SMD:R_0402_1005Metric -> Resistor_SMD:R_0805_2012Metric
- R53: renamed from R33; footprint Resistor_SMD:R_0402_1005Metric -> Resistor_SMD:R_0805_2012Metric
- R54: renamed from R34; footprint Resistor_SMD:R_0402_1005Metric -> Resistor_SMD:R_0805_2012Metric
- R55: renamed from R35; footprint Resistor_SMD:R_0402_1005Metric -> Resistor_SMD:R_0805_2012Metric
- R56: renamed from R36; footprint Resistor_SMD:R_0402_1005Metric -> Resistor_SMD:R_0805_2012Metric
- R57: renamed from R37; footprint Resistor_SMD:R_0402_1005Metric -> Resistor_SMD:R_0805_2012Metric
- R58: renamed from R38; footprint Resistor_SMD:R_0402_1005Metric -> Resistor_SMD:R_0805_2012Metric
- R59: renamed from R39; footprint Resistor_SMD:R_0402_1005Metric -> Resistor_SMD:R_0805_2012Metric
- R60: renamed from R40; value R -> 45k; footprint Resistor_SMD:R_0402_1005Metric -> Resistor_SMD:R_0805_2012Metric
- R61: renamed from R41; value R -> 10k; footprint Resistor_SMD:R_0402_1005Metric -> Resistor_SMD:R_0805_2012Metric
- R62: renamed from R42; value R -> 10k; footprint Resistor_SMD:R_0402_1005Metric -> Resistor_SMD:R_0805_2012Metric
- R63: renamed from R43; value R -> 10k; footprint Resistor_SMD:R_0402_1005Metric -> Resistor_SMD:R_0805_2012Metric
- R64: renamed from R44; footprint Resistor_SMD:R_1206_3216Metric -> Resistor_SMD:R_0805_2012Metric
- R65: renamed from R45; footprint Resistor_SMD:R_1206_3216Metric -> Resistor_SMD:R_0805_2012Metric
- R66: renamed from R46; footprint Resistor_SMD:R_1206_3216Metric -> Resistor_SMD:R_0805_2012Metric
- R67: renamed from R47; footprint Resistor_SMD:R_1206_3216Metric -> Resistor_SMD:R_0805_2012Metric
- R68: renamed from R48; footprint Resistor_SMD:R_1206_3216Metric -> Resistor_SMD:R_0805_2012Metric
- R70: renamed from R50; footprint Resistor_SMD:R_1206_3216Metric -> Resistor_SMD:R_0805_2012Metric
- R71: renamed from R51; footprint Resistor_SMD:R_1206_3216Metric -> Resistor_SMD:R_0805_2012Metric
- R74: renamed from R54; footprint Resistor_SMD:R_0402_1005Metric -> Resistor_SMD:R_0805_2012Metric
- R75: renamed from R55; footprint Resistor_SMD:R_0402_1005Metric -> Resistor_SMD:R_0805_2012Metric
- R76: renamed from R56; footprint Resistor_SMD:R_0402_1005Metric -> Resistor_SMD:R_0805_2012Metric
- R77: renamed from R57; footprint Resistor_SMD:R_0402_1005Metric -> Resistor_SMD:R_0805_2012Metric
- R78: renamed from R58; footprint Resistor_SMD:R_0402_1005Metric -> Resistor_SMD:R_0805_2012Metric
- R79: renamed from R59; footprint Resistor_SMD:R_0402_1005Metric -> Resistor_SMD:R_0805_2012Metric
- R80: renamed from R60; footprint Resistor_SMD:R_0402_1005Metric -> Resistor_SMD:R_0805_2012Metric
- R81: renamed from R61; footprint Resistor_SMD:R_0402_1005Metric -> Resistor_SMD:R_0805_2012Metric
- R82: renamed from R62; footprint Resistor_SMD:R_0402_1005Metric -> Resistor_SMD:R_0805_2012Metric
- R9: renamed from R7; value 22 -> 27
- moved R62 58.6 mm to (114.0, 85.9)
- moved R9 2.53 mm to (86.0, 34.4)
- renumbered C9 to C10, C10 to C11, C11 to C12, C7 to C13, C12 to C14, C13 to C15, C14 to C16, C15 to C17, C34 to C36, C35 to C37, C36 to C38, C37 to C39, C2 to C4, C38 to C40, C39 to C41, C40 to C42, C41 to C43, C3 to C5, C4 to C6, C5 to C7, C6 to C8, C8 to C9, D4 to D3, D3 to D4, J1 to J14, J2 to J16, J3 to J17, J4 to J18, R22 to R36, R23 to R37, R24 to R44, R25 to R45, R21 to R5, R20 to R6, R49 to R69, R5 to R7, R52 to R72, R53 to R73, R6 to R8, U9 to U10, U10 to U11, U11 to U12, U2 to U3, U3 to U4, U4 to U5, U5 to U6, U6 to U7, U7 to U8, U8 to U9
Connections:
- D3 pad 1: /GW1NR FPGA/MIDI-LED-in -> /RP2040 microcontroller/MIDI-LED-out
- D4 pad 1: /GW1NR FPGA/MIDI-LED-out -> /RP2040 microcontroller/MIDI-LED-in
- R44 pad 1: /GW1NR FPGA/FLASH_CS -> /RP2040 microcontroller/FLASH-CS
- U1 pad 1: /GW1NR FPGA/FLASH_CS -> Net-(R31-Pad2)
- U1 pad 2: /GW1NR FPGA/FLASH-SIO1 -> Net-(R34-Pad2)
- U1 pad 3: /GW1NR FPGA/FLASH-SIO2 -> Net-(R32-Pad2)
- U1 pad 5: /GW1NR FPGA/FLASH-SIO0 -> Net-(R29-Pad2)
- U1 pad 6: /GW1NR FPGA/FLASH-SCLK -> Net-(R30-Pad2)
- U1 pad 7: /GW1NR FPGA/FLASH-SIO3 -> Net-(R33-Pad2)
- U3 pad 17: unconnected-(U2-Pad17) -> /RP2040 microcontroller/spare7
- U3 pad 18: unconnected-(U2-Pad18) -> /RP2040 microcontroller/MIDI-LED-out
- U3 pad 21: unconnected-(U2-Pad21) -> Net-(J7-Pad1)
- U3 pad 24: unconnected-(U2-Pad24) -> Net-(J5-Pad1)
- U3 pad 25: unconnected-(U2-Pad25) -> Net-(J6-Pad1)
- U3 pad 27: unconnected-(U2-Pad27) -> /RP2040 microcontroller/MIDI-LED-in
- U3 pad 28: unconnected-(U2-Pad28) -> Net-(J8-Pad1)
- U3 pad 29: unconnected-(U2-Pad29) -> Net-(J9-Pad1)
- U3 pad 38: unconnected-(U2-Pad38) -> Net-(J10-Pad1)
- U3 pad 39: unconnected-(U2-Pad39) -> Net-(J11-Pad1)
- U3 pad 40: unconnected-(U2-Pad40) -> Net-(J12-Pad1)
- U3 pad 41: unconnected-(U2-Pad41) -> Net-(J13-Pad1)
- U3 pad 51: /GW1NR FPGA/FLASH-SIO3 -> /RP2040 microcontroller/FLASH-SIO3
- U3 pad 52: /GW1NR FPGA/FLASH-SCLK -> /RP2040 microcontroller/FLASH-SCLK
- U3 pad 53: /GW1NR FPGA/FLASH-SIO0 -> /RP2040 microcontroller/FLASH-SIO0
- U3 pad 54: /GW1NR FPGA/FLASH-SIO2 -> /RP2040 microcontroller/FLASH-SIO2
- U3 pad 55: /GW1NR FPGA/FLASH-SIO1 -> /RP2040 microcontroller/FLASH-SIO1
- U3 pad 56: /GW1NR FPGA/FLASH_CS -> /RP2040 microcontroller/FLASH-CS
- U6 pad 3: /GW1NR FPGA/FLASH_CS -> Net-(J15-Pad1)
- U6 pad 59: /GW1NR FPGA/MIDI-LED-out -> /GW1NR FPGA/spare7
- U6 pad 60: /GW1NR FPGA/MIDI-LED-in -> /GW1NR FPGA/FLASH-CS
